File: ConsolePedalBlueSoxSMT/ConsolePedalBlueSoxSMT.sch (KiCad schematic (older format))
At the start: 51 parts, among them IC1 CD4013BE, J1 Conn_02x25_Counter_Clockwise, Q1 2N3904, Q2 2N3904, Q3 2N3904, U1 RC4558

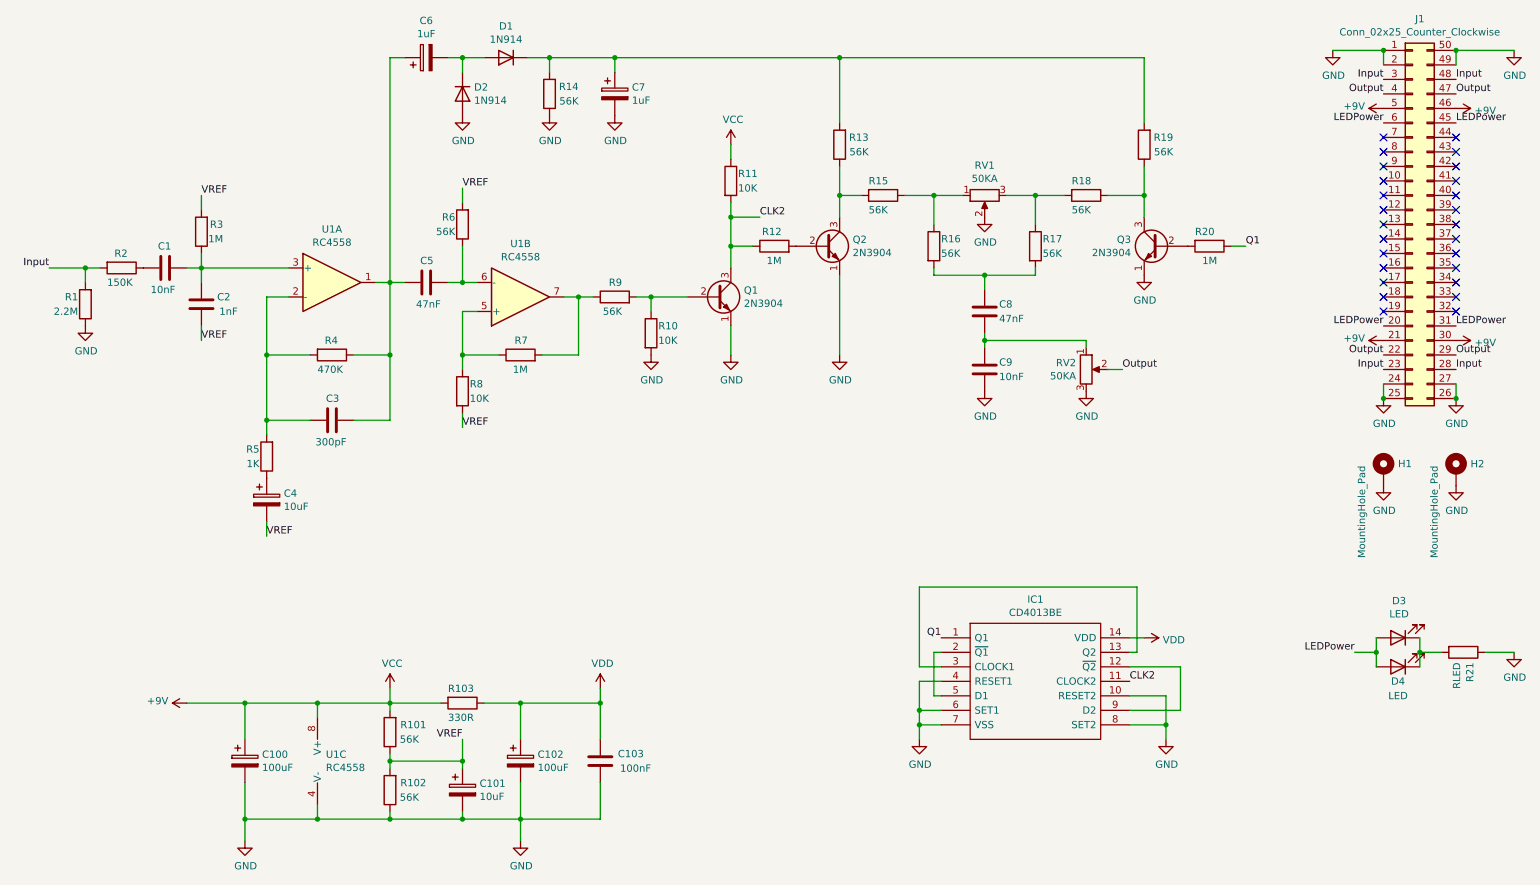
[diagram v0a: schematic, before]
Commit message: Finished assigning footprints
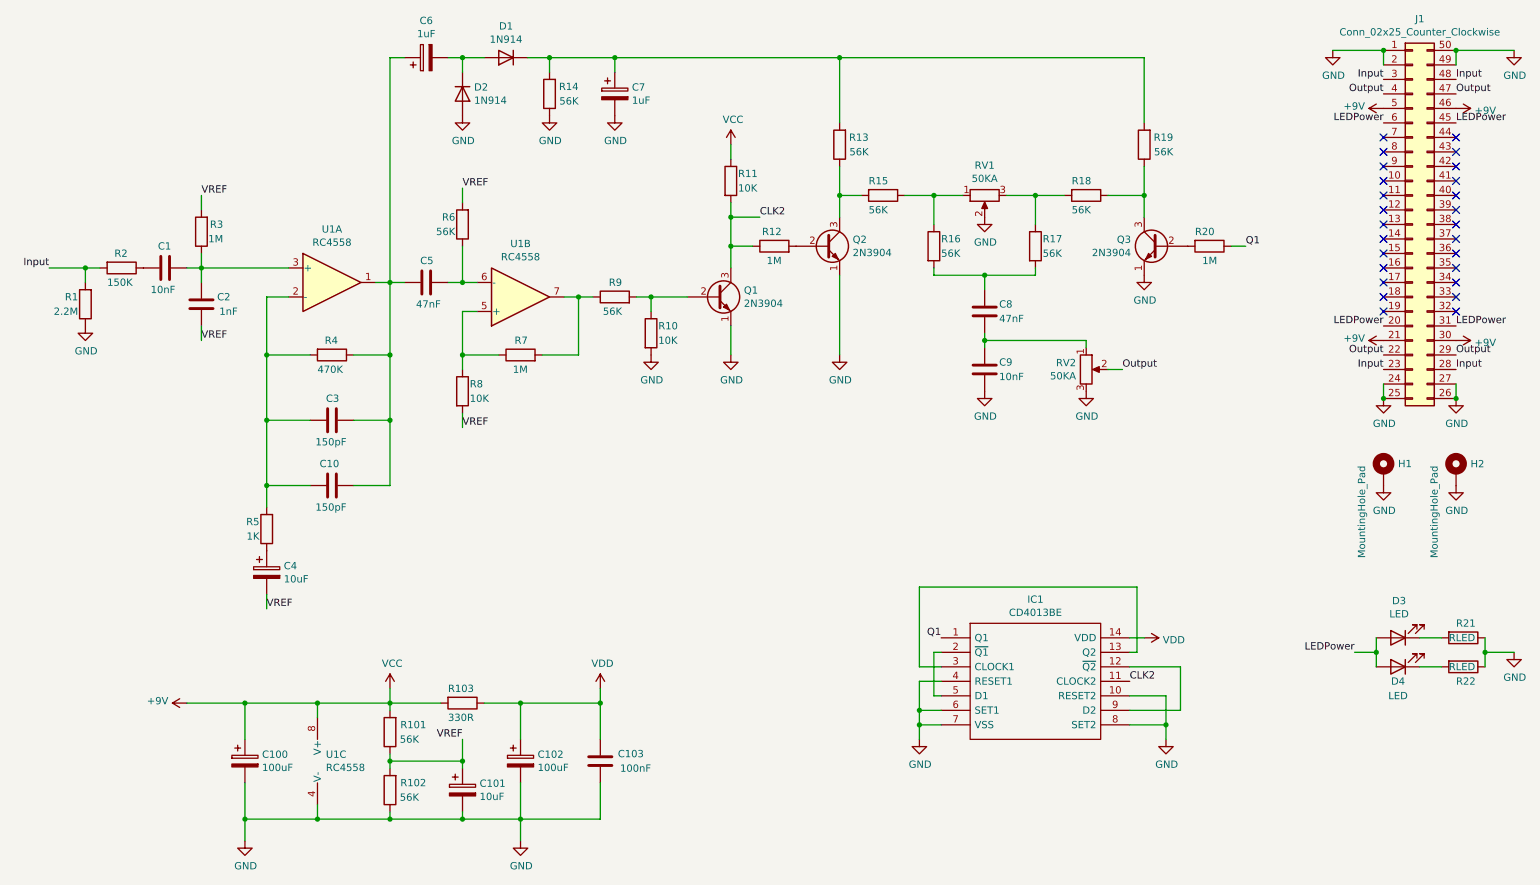
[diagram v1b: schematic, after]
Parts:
- added C10: 150pF, Capacitor_SMD:C_0603_1608Metric, symbol Device:C
- added R22: RLED, Resistor_THT:R_Axial_DIN0207_L6.3mm_D2.5mm_P10.16mm_Horizontal, symbol Device:R
- C1, C9: footprint libraries:C_Flat_L7.2_H6.5 -> Capacitor_SMD:C_0603_1608Metric; LCSC (none) -> C57112
- C100: footprint libraries:CP_Radial_D6.3mm_P2.50mm_L11.0mm -> Capacitor_SMD:CP_Elec_6.3x5.3; LCSC (none) -> C176674
- C101, C4: footprint libraries:CP_Radial_D6.3mm_P2.50mm -> Capacitor_SMD:CP_Elec_4x5.4; LCSC (none) -> C72485
- C102: footprint libraries:CP_Radial_D6.3mm_P2.50mm_L11.0mm -> Capacitor_SMD:CP_Elec_4x5.4; LCSC (none) -> C176674
- C103: footprint libraries:C_Flat_L7.2_H6.5 -> Capacitor_SMD:C_0603_1608Metric; LCSC (none) -> C14663
- C2: footprint libraries:C_Flat_L7.2_H6.5 -> Capacitor_SMD:C_0603_1608Metric; LCSC (none) -> C1588
- C3: value 300pF -> 150pF; footprint libraries:C_Flat_L7.2_H6.5 -> Capacitor_SMD:C_0603_1608Metric; LCSC (none) -> C1594
- C5, C8: footprint libraries:C_Flat_L7.2_H6.5 -> Capacitor_SMD:C_0603_1608Metric; LCSC (none) -> C1622
- C6, C7: footprint libraries:CP_Radial_D5.0mm_P2.00mm_L11.0mm -> Capacitor_SMD:CP_Elec_4x5.4; LCSC (none) -> C3348
- D1, D2: footprint Diode_THT:D_DO-35_SOD27_P7.62mm_Horizontal -> Diode_SMD:D_SOD-323F; LCSC (none) -> C258181
- IC1: footprint Package_DIP:DIP-14_W7.62mm -> Package_SO:SOIC-14_3.9x8.7mm_P1.27mm; LCSC (none) -> C13527
- Q1, Q2, Q3: footprint Package_TO_SOT_THT:TO-92_Inline -> Package_TO_SOT_SMD:SOT-23; LCSC (none) -> C20526
- R10, R11, R8: footprint Resistor_THT:R_Axial_DIN0207_L6.3mm_D2.5mm_P10.16mm_Horizontal -> Resistor_SMD:R_0603_1608Metric; LCSC (none) -> C25804
- R101, R102, R14, R15, R16, R17, R18, R19: footprint Resistor_THT:R_Axial_DIN0207_L6.3mm_D2.5mm_P10.16mm_Horizontal -> Resistor_SMD:R_0603_1608Metric; LCSC (none) -> C23206
- R103: footprint Resistor_THT:R_Axial_DIN0207_L6.3mm_D2.5mm_P10.16mm_Horizontal -> Resistor_SMD:R_0603_1608Metric; LCSC (none) -> C23138
- U1: footprint Package_DIP:DIP-8_W7.62mm -> Package_SO:SOIC-8_3.9x4.9mm_P1.27mm; LCSC (none) -> C7457
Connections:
- net GND: now also R22.1
- net at D3.1 (K), R21.2: no longer D4.1 (K)
- net at C3.2, C5.1, C6.1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: now also C10.2
- net at C3.1, R4.2, R5.2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: now also C10.1
- new net: D4.1 (K), R22.2
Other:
- moved on the sheet: C4, R21, R5

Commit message: Fixed incorrect footprint and exported everything again
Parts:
- C102: footprint Capacitor_SMD:CP_Elec_4x5.4 -> Capacitor_SMD:CP_Elec_6.3x5.3
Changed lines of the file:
@@
 F 0 "C102" H 4218 5896 50  0000 L CNN
 F 1 "100uF" H 4218 5805 50  0000 L CNN
-F 2 "Capacitor_SMD:CP_Elec_4x5.4" H 4138 5700 50  0001 C CNN
+F 2 "Capacitor_SMD:CP_Elec_6.3x5.3" H 4138 5700 50  0001 C CNN
 F 3 "~" H 4100 5850 50  0001 C CNN
 F 4 "C176674" H 4100 5850 50  0001 C CNN "LCSC"
